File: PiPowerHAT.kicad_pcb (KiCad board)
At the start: 2 copper layers, 65 x 56 mm, 42 parts, among them J1 MSTB, J10 GMSTB, J2 Conn_01x03, J3 Conn_01x02, J5 Conn_01x06, J6 Raspberry_Pi_2_3, J7 Conn_02x03_Odd_Even, J9 Conn_01x04_Male, Q1 AO3401A, Q2 MMDT5401, Q3 DMG2305UX-13, U1 XL4015, U2 CAT24C32

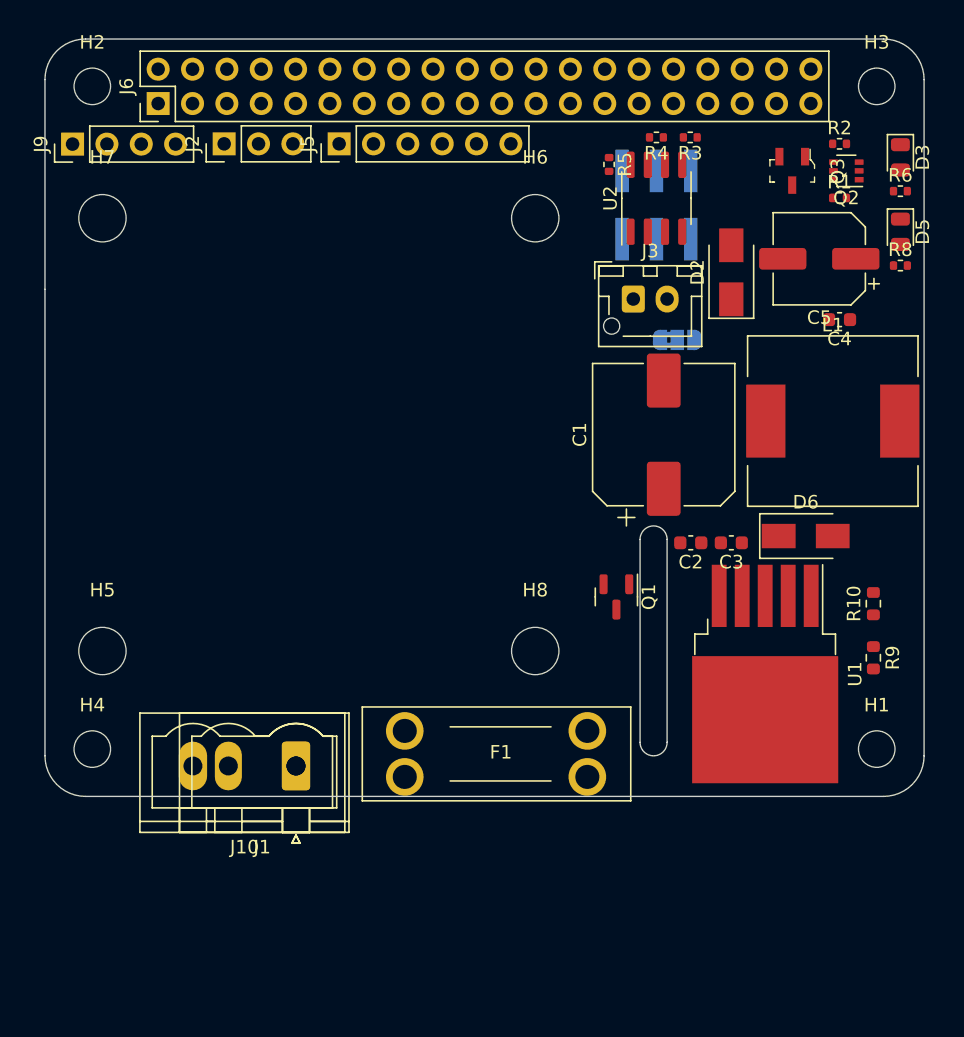
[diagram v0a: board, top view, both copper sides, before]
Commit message: changed out fuseholder, mounting holes, headers, removed i2c, etc
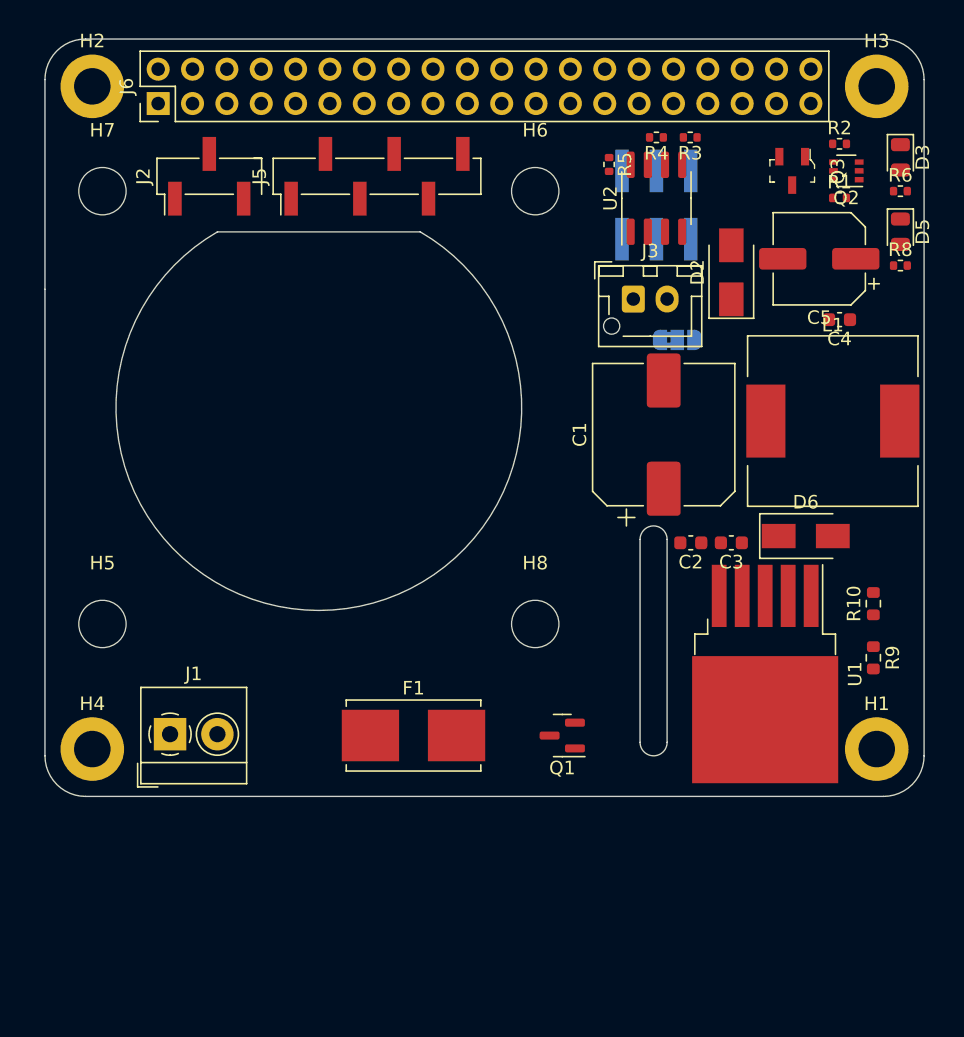
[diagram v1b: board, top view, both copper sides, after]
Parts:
- removed J10: GMSTB, Connector_Phoenix_GMSTB:PhoenixContact_GMSTBVA_2,5_2-G-7,62_1x02_P7.62mm_Vertical
- removed J9: Conn_01x04_Male, Connector_PinHeader_2.54mm:PinHeader_1x04_P2.54mm_Vertical
- F1: footprint Fuse:Fuseholder_Blade_Keystone_3557-2 -> Fuse:Fuseholder_Littelfuse_Nano2_154x
- H1, H2, H3, H4: footprint MountingHole:MountingHole_2.7mm_M2.5_ISO14580 -> MountingHole:MountingHole_2.7mm_M2.5_DIN965_Pad
- J1: value MSTB -> 2444; footprint Connector_Phoenix_MSTB:PhoenixContact_MSTBVA_2,5_2-G_1x02_P5.00mm_Vertical -> TerminalBlock_4Ucon:TerminalBlock_4Ucon_1x02_P3.50mm_Horizontal
- J2: footprint Connector_PinHeader_2.54mm:PinHeader_1x03_P2.54mm_Vertical -> Connector_PinHeader_2.54mm:PinHeader_1x03_P2.54mm_Vertical_SMD_Pin1Left
- J5: footprint Connector_PinHeader_2.54mm:PinHeader_1x06_P2.54mm_Vertical -> Connector_PinHeader_2.54mm:PinHeader_1x06_P2.54mm_Vertical_SMD_Pin1Left
- moved Q1 11.0 mm to (123.5, 104.8), turned to 180 degrees
- moved J1 9.60 mm to (94.5, 104.7), turned to 0 degrees
- moved F1 4.54 mm to (112.5, 104.8)
- moved J5 3.69 mm to (109.8, 63.4)
- moved J2 2.64 mm to (97.4, 63.4)
- moved H5 2.00 mm to (89.5, 96.5)
- moved H6 2.00 mm to (121.5, 64.5)
- moved H7 2.00 mm to (89.5, 64.5)
- moved H8 2.00 mm to (121.5, 96.5)
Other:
- outline, holes or cut-outs redrawn

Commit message: Layout V1 complete
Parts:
- J3: footprint Connector_JST:JST_XH_B2B-XH-AM_1x02_P2.50mm_Vertical -> Connector_JST:JST_XH_S2B-XH-A_1x02_P2.50mm_Horizontal; moved to B.Cu
- moved R3 7.26 mm to (126.2, 63.0), turned to -90 degrees
- moved R4 6.47 mm to (126.2, 65.3), turned to -90 degrees
- moved R5 4.99 mm to (126.2, 67.5), turned to 90 degrees
- moved JP1 4.30 mm to (136.3, 75.5)
- moved J3 2.43 mm to (131.1, 73.2), turned to 180 degrees
- moved D5 2.40 mm to (148.5, 69.9)
- moved R8 2.25 mm to (148.5, 72.2), turned to 180 degrees
- moved D3 1.85 mm to (148.5, 63.9)
- moved R6 1.85 mm to (148.5, 66.3), turned to 180 degrees
- moved R1 1.03 mm to (143.0, 65.2), turned to 180 degrees
- moved R9 0.79 mm to (147.2, 98.8)
- moved C4 0.75 mm to (143.2, 74.0)
- moved R10 0.75 mm to (147.2, 95.0)
- moved Q3 0.60 mm to (140.5, 62.4)
- moved U2 0.47 mm to (130.5, 65.5), turned to 180 degrees
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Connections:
- J6 pad 1: +3V3 -> unconnected-(J6-Pad1)
- J6 pad 3: SDA -> unconnected-(J6-Pad3)
- J6 pad 5: SCL -> unconnected-(J6-Pad5)
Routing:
- net +3V3: track 0.00 -> 41.8 mm, vias 0 -> 2
- net VCC: track 0.00 -> 24.3 mm, vias 0 -> 2
- net ID_SC: track 0.00 -> 22.5 mm, vias 0 -> 1
- net Net-(D6-Pad1): track 0.00 -> 22.1 mm
- net CS: track 0.00 -> 20.3 mm, vias 0 -> 2
- net RX: track 0.00 -> 12.8 mm
- net Net-(D2-Pad1): track 0.00 -> 12.7 mm, vias 0 -> 1
- net Net-(R10-Pad1): track 0.00 -> 12.1 mm
- net +5V: track 0.00 -> 11.3 mm, vias 0 -> 1
- net MISO: track 0.00 -> 11.0 mm
- net ID_SD: track 0.00 -> 9.97 mm, vias 0 -> 1
- net GND: track 0.00 -> 8.30 mm, vias 0 -> 50
- net MOSI: track 0.00 -> 7.57 mm
- net SCLK: track 0.00 -> 6.46 mm
- net TX: track 0.00 -> 6.40 mm
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- added copper zone on F.Cu, net +5V
- added copper zone on F.Cu, net 5V_PI
- added copper zone on B.Cu, net GND
- added copper zone on F.Cu, net GND
- added copper zone on F.Cu, net Net-(F1-Pad1)
- added copper zone on F.Cu, net Net-(F1-Pad2)
- added copper zone on F.Cu, net VCC
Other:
- board text added: "+"
- board text added: "+3V3"
- board text added: "-"
- board text added: "3V3"
- board text added: "5V"
- board text added: "CS"
- board text added: "Design by Sreenivas Eadara"
- board text added: "GND"
- board text added: "MISO"
- board text added: "MOSI"
- board text added: "NC"
- board text added: "RX"
- board text added: "SC"
- board text added: "SCLK"
- board text added: "SD"
- board text added: "TX"
- board text added: "VCC"
- board text added: "WP"

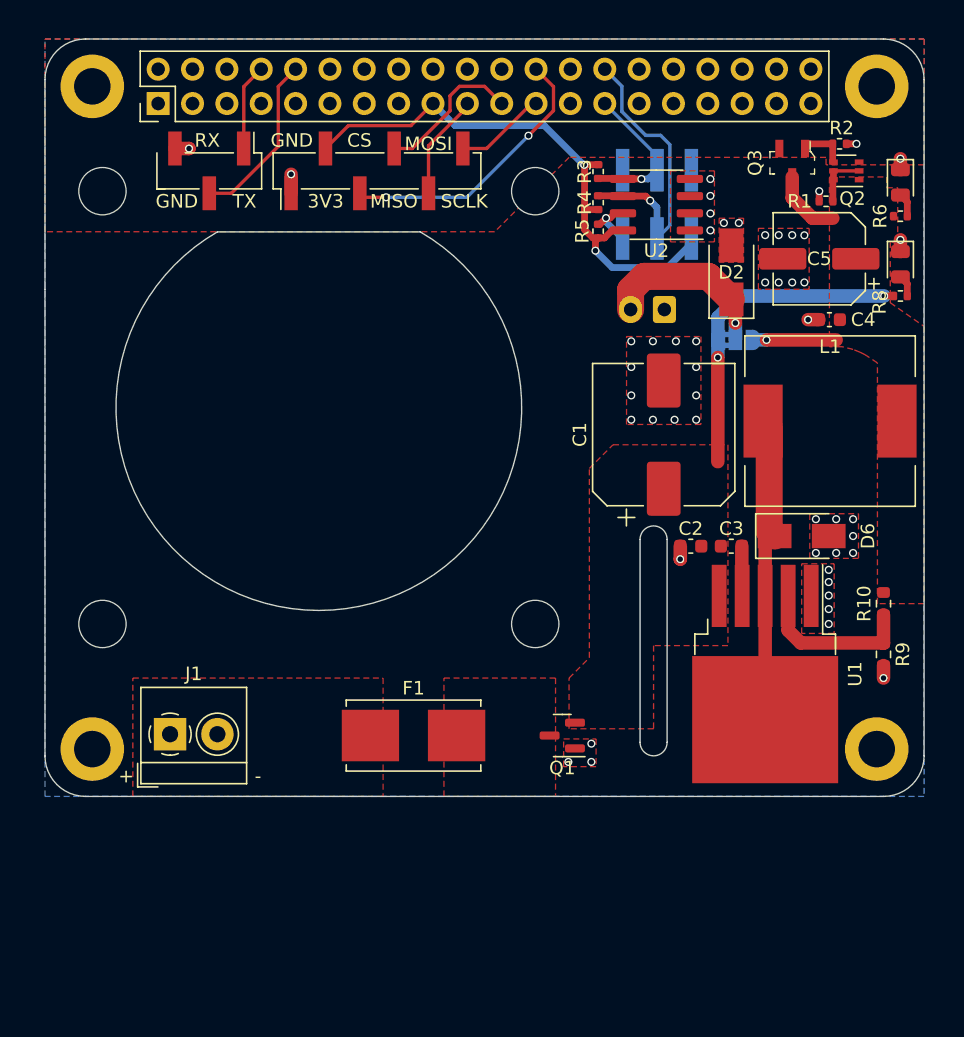
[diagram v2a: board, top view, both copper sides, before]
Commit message: Adding panelization between breakouts. Updated layout and component position.
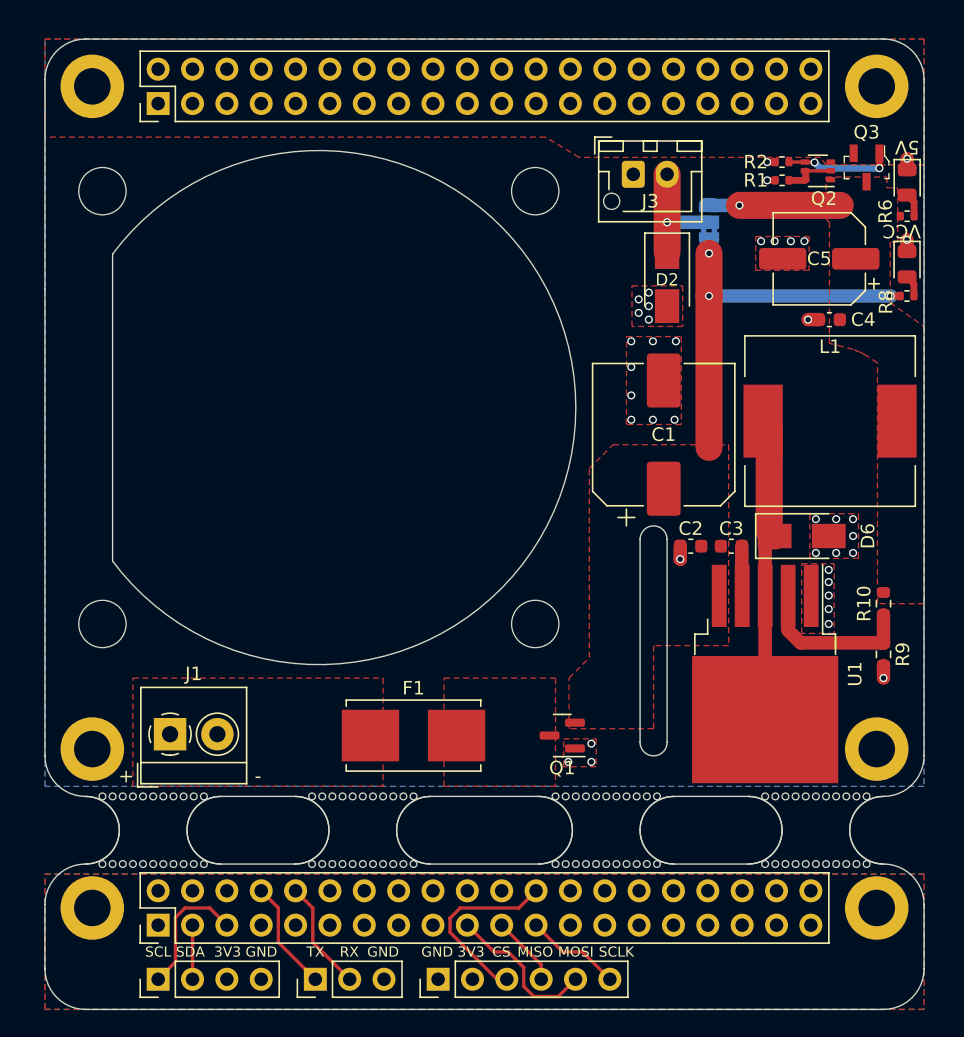
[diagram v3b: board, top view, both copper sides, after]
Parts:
- removed R3, R4: 3.9K, Resistor_SMD:R_0402_1005Metric
- removed R5: 1K, Resistor_SMD:R_0402_1005Metric
- removed U2: CAT24C32, Package_SO:SOIC-8_3.9x4.9mm_P1.27mm
- added H10: MountingHole, MountingHole:MountingHole_2.7mm_M2.5_DIN965_Pad, F.Cu at (146.8, 117.5)
- added H9: MountingHole, MountingHole:MountingHole_2.7mm_M2.5_DIN965_Pad, F.Cu at (88.8, 117.5)
- added J4: Conn_01x06, Connector_PinHeader_2.54mm:PinHeader_1x06_P2.54mm_Vertical, F.Cu at (114.3, 122.8)
- added mouse-bite-3mm-slot: VAL**, Panelization:mouse-bite-5mm-slot, F.Cu at (142.2, 111.8)
- added mouse-bite-3mm-slot: VAL**, Panelization:mouse-bite-5mm-slot, F.Cu at (93.2, 111.8)
- added mouse-bite-3mm-slot: VAL**, Panelization:mouse-bite-5mm-slot, F.Cu at (108.8, 111.8)
- added mouse-bite-3mm-slot: VAL**, Panelization:mouse-bite-5mm-slot, F.Cu at (126.8, 111.8)
- J2: value Conn_01x03 -> Raspberry_Pi_2_3; footprint Connector_PinHeader_2.54mm:PinHeader_1x03_P2.54mm_Vertical_SMD_Pin1Left -> Connector_PinHeader_2.54mm:PinHeader_2x20_P2.54mm_Vertical
- J3: footprint Connector_JST:JST_XH_S2B-XH-A_1x02_P2.50mm_Horizontal -> Connector_JST:JST_XH_B2B-XH-AM_1x02_P2.50mm_Vertical; moved to F.Cu
- J5: value Conn_01x06 -> Conn_01x04; footprint Connector_PinHeader_2.54mm:PinHeader_1x06_P2.54mm_Vertical_SMD_Pin1Left -> Connector_PinHeader_2.54mm:PinHeader_1x04_P2.54mm_Vertical
- J7: value Conn_02x03_Odd_Even -> Conn_01x03; footprint Connector_PinHeader_2.54mm:PinHeader_2x03_P2.54mm_Vertical_SMD -> Connector_PinHeader_2.54mm:PinHeader_1x03_P2.54mm_Vertical; moved to F.Cu
- moved J7 62.6 mm to (105.2, 122.8)
- moved J5 61.9 mm to (93.6, 122.8)
- moved J2 55.9 mm to (93.6, 118.8), turned to 90 degrees
- moved J3 10.3 mm to (128.8, 63.2), turned to 0 degrees
- moved JP1 8.92 mm to (134.3, 66.8), turned to 90 degrees
- moved Q3 5.51 mm to (146.0, 62.8)
- moved D2 4.78 mm to (131.2, 71.0), turned to -90 degrees
- moved R2 4.46 mm to (139.8, 62.4), turned to 180 degrees
- moved R1 3.60 mm to (139.8, 63.7)
- moved Q2 2.10 mm to (142.4, 63.0)
- moved D3 0.50 mm to (149.0, 63.9)
- moved R6 0.50 mm to (149.0, 66.3)
- moved D5 0.49 mm to (149.0, 69.9)
- moved R8 0.49 mm to (149.0, 72.2)
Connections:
- J2 pad 1: TX -> +3V3
- J2 pad 2: RX -> unconnected-(J2-Pad2)
- J2 pad 3: GND -> SDA
- J5 pad 1: GND -> SCL
- J5 pad 2: +3V3 -> SDA
- J5 pad 3: CS -> +3V3
- J5 pad 4: MISO -> GND1
- J6 pad 10: RX -> unconnected-(J6-Pad10)
- J6 pad 17: +3V3 -> unconnected-(J6-Pad17)
- J6 pad 19: MOSI -> unconnected-(J6-Pad19)
- J6 pad 21: MISO -> unconnected-(J6-Pad21)
- J6 pad 23: SCLK -> unconnected-(J6-Pad23)
- J6 pad 24: CS -> unconnected-(J6-Pad24)
- J6 pad 27: ID_SD -> unconnected-(J6-Pad27)
- J6 pad 28: ID_SC -> unconnected-(J6-Pad28)
- J6 pad 8: TX -> unconnected-(J6-Pad8)
- J7 pad 1: +3V3 -> TX
- J7 pad 2: GND -> RX
- J7 pad 3: ID_SC -> GND1
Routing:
- net +3V3: track 41.8 -> 0.00 mm, vias 2 -> 0
- net ID_SC: track 22.5 -> 0.00 mm, vias 1 -> 0
- net ID_SD: track 9.97 -> 0.00 mm, vias 1 -> 0
- net SCL: track 0.00 -> 9.72 mm
- net CS: track 20.3 -> 13.9 mm, vias 2 -> 0
- net MISO: track 11.0 -> 5.21 mm
- net VCC: track 24.3 -> 29.5 mm, vias 2 -> 3
- net RX: track 12.8 -> 8.20 mm
- net Net-(Q2-Pad4): track 3.56 -> 7.98 mm, vias 0 -> 2
- net Net-(D2-Pad1): track 12.7 -> 8.45 mm
- net SDA: track 0.00 -> 4.00 mm
- net MOSI: track 7.57 -> 11.5 mm
- net WP: track 3.59 -> 0.00 mm, vias 1 -> 0
- net GND: track 8.30 -> 5.54 mm, vias 50 -> 39
- net TX: track 6.40 -> 8.20 mm
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- added copper zone on F.Cu, net +3V3
- added copper zone on B.Cu, net GND1
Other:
- board size 65 x 56 mm -> 65 x 71.8 mm
- board text added: "SCL"
- board text added: "SDA"
- board text added: "Vector 3D PowerPi Designed by Sreenivas Eadara"
- board text removed: "+3V3"
- board text removed: "Design by Sreenivas Eadara"
- board text removed: "NC"
- board text removed: "SC"
- board text removed: "SD"
- board text removed: "WP"

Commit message: remove breakout board and add +5V out
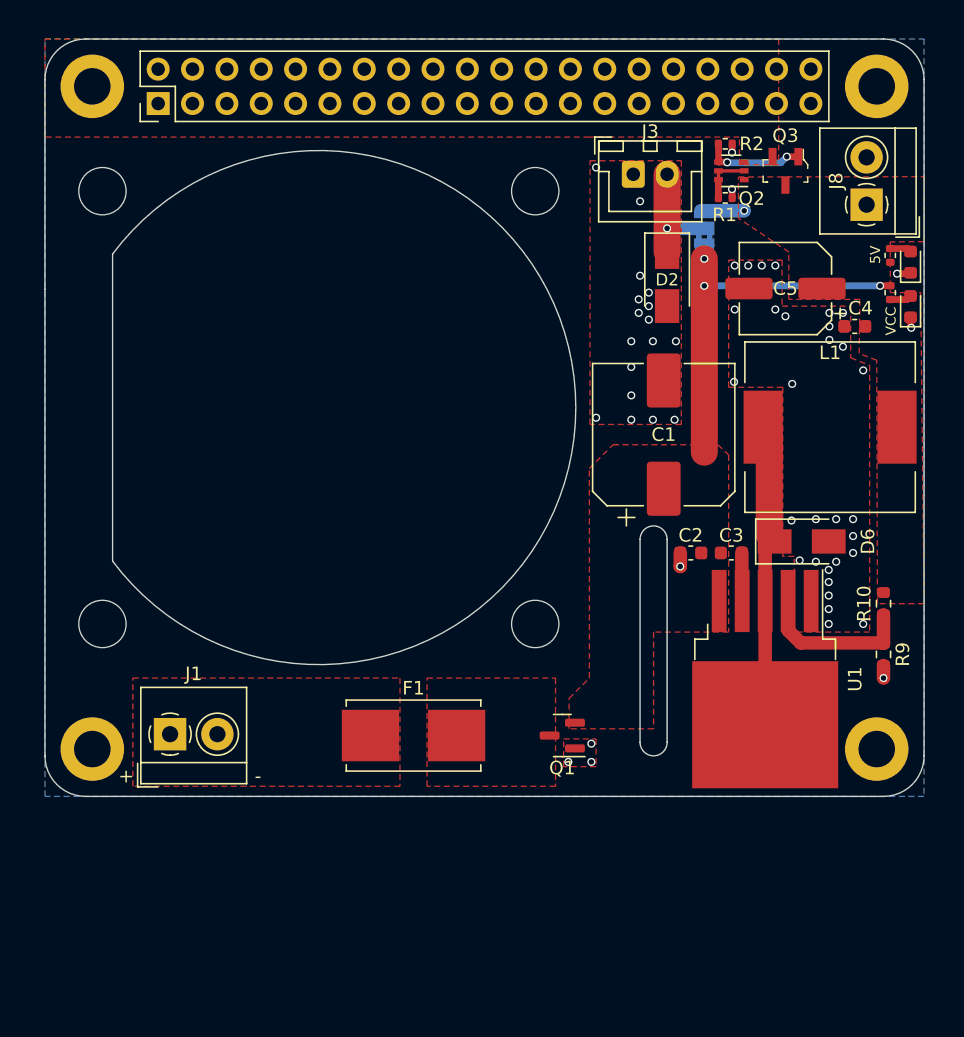
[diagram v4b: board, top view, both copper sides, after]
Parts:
- removed H10, H9: MountingHole, MountingHole:MountingHole_2.7mm_M2.5_DIN965_Pad
- removed J2: Raspberry_Pi_2_3, Connector_PinHeader_2.54mm:PinHeader_2x20_P2.54mm_Vertical
- removed J4: Conn_01x06, Connector_PinHeader_2.54mm:PinHeader_1x06_P2.54mm_Vertical
- removed J5: Conn_01x04, Connector_PinHeader_2.54mm:PinHeader_1x04_P2.54mm_Vertical
- removed J7: Conn_01x03, Connector_PinHeader_2.54mm:PinHeader_1x03_P2.54mm_Vertical
- removed mouse-bite-3mm-slot (x4): VAL**, Panelization:mouse-bite-5mm-slot
- added J8: 2444, TerminalBlock_4Ucon:TerminalBlock_4Ucon_1x02_P3.50mm_Horizontal, F.Cu at (146.0, 65.5)
- D3, D5: value C2297 -> C72038; footprint LED_SMD:LED_0805_2012Metric -> LED_SMD:LED_0603_1608Metric
- J3: footprint Connector_JST:JST_XH_B2B-XH-AM_1x02_P2.50mm_Vertical -> Connector_JST:JST_XH_B2B-XH-A_1x02_P2.50mm_Vertical
- moved Q2 6.40 mm to (136.0, 63.0)
- moved Q3 6.01 mm to (140.0, 63.0)
- moved D3 5.91 mm to (149.2, 69.8), turned to 90 degrees
- moved R2 4.41 mm to (135.6, 61.0), turned to 0 degrees
- moved R1 4.40 mm to (135.6, 65.0), turned to 0 degrees
- moved C5 3.33 mm to (140.0, 71.7)
- moved R6 3.16 mm to (147.8, 69.2), turned to -90 degrees
- moved D5 3.15 mm to (149.2, 73.0), turned to 90 degrees
- moved C4 1.94 mm to (145.1, 74.5)
- moved R8 1.26 mm to (147.8, 72.0), turned to 90 degrees
- moved JP1 0.57 mm to (134.0, 67.2)
- moved C2 0.50 mm to (133.0, 91.2)
- moved C3 0.50 mm to (136.0, 91.2)
- moved L1 0.45 mm to (143.3, 82.0)
- moved D6 0.40 mm to (141.2, 90.4)
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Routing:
- net CS: track 13.9 -> 0.00 mm
- net MOSI: track 11.5 -> 0.00 mm
- net SCL: track 9.72 -> 0.00 mm
- net TX: track 8.20 -> 0.00 mm
- net RX: track 8.20 -> 0.00 mm
- net SCLK: track 7.12 -> 0.00 mm
- net +5V: track 9.65 -> 2.95 mm
- net MISO: track 5.21 -> 0.00 mm
- net SDA: track 4.00 -> 0.00 mm
- net Net-(Q2-Pad4): track 7.98 -> 7.46 mm
- net Net-(C3-Pad1): track 3.65 -> 3.15 mm
- net GND: track 5.54 -> 5.06 mm, vias 39 -> 56
- removed copper zone on F.Cu, net +3V3
- removed copper zone on B.Cu, net GND1
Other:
- board size 65 x 71.8 mm -> 65 x 56 mm
- board text removed: "3V3"
- board text removed: "CS"
- board text removed: "GND"
- board text removed: "MISO"
- board text removed: "MOSI"
- board text removed: "RX"
- board text removed: "SCL"
- board text removed: "SCLK"
- board text removed: "SDA"
- board text removed: "TX"
